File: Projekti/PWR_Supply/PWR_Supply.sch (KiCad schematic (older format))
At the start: 0 parts

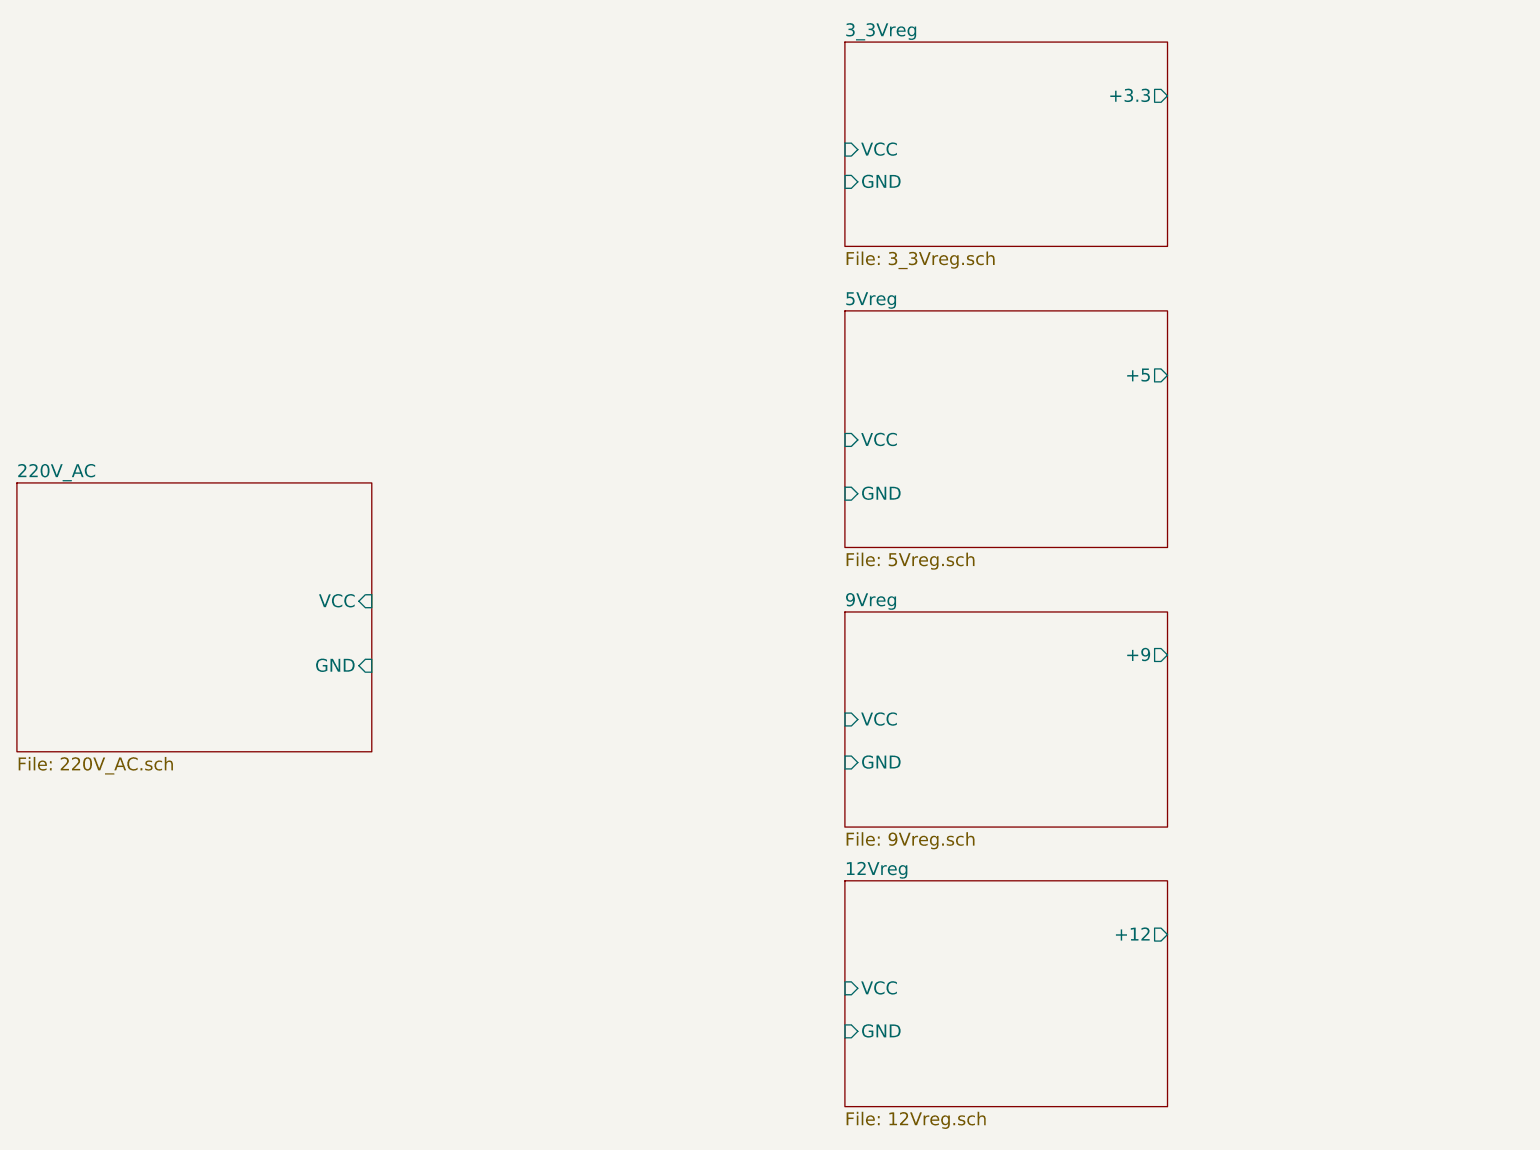
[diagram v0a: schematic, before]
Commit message: Savienojaam pin's
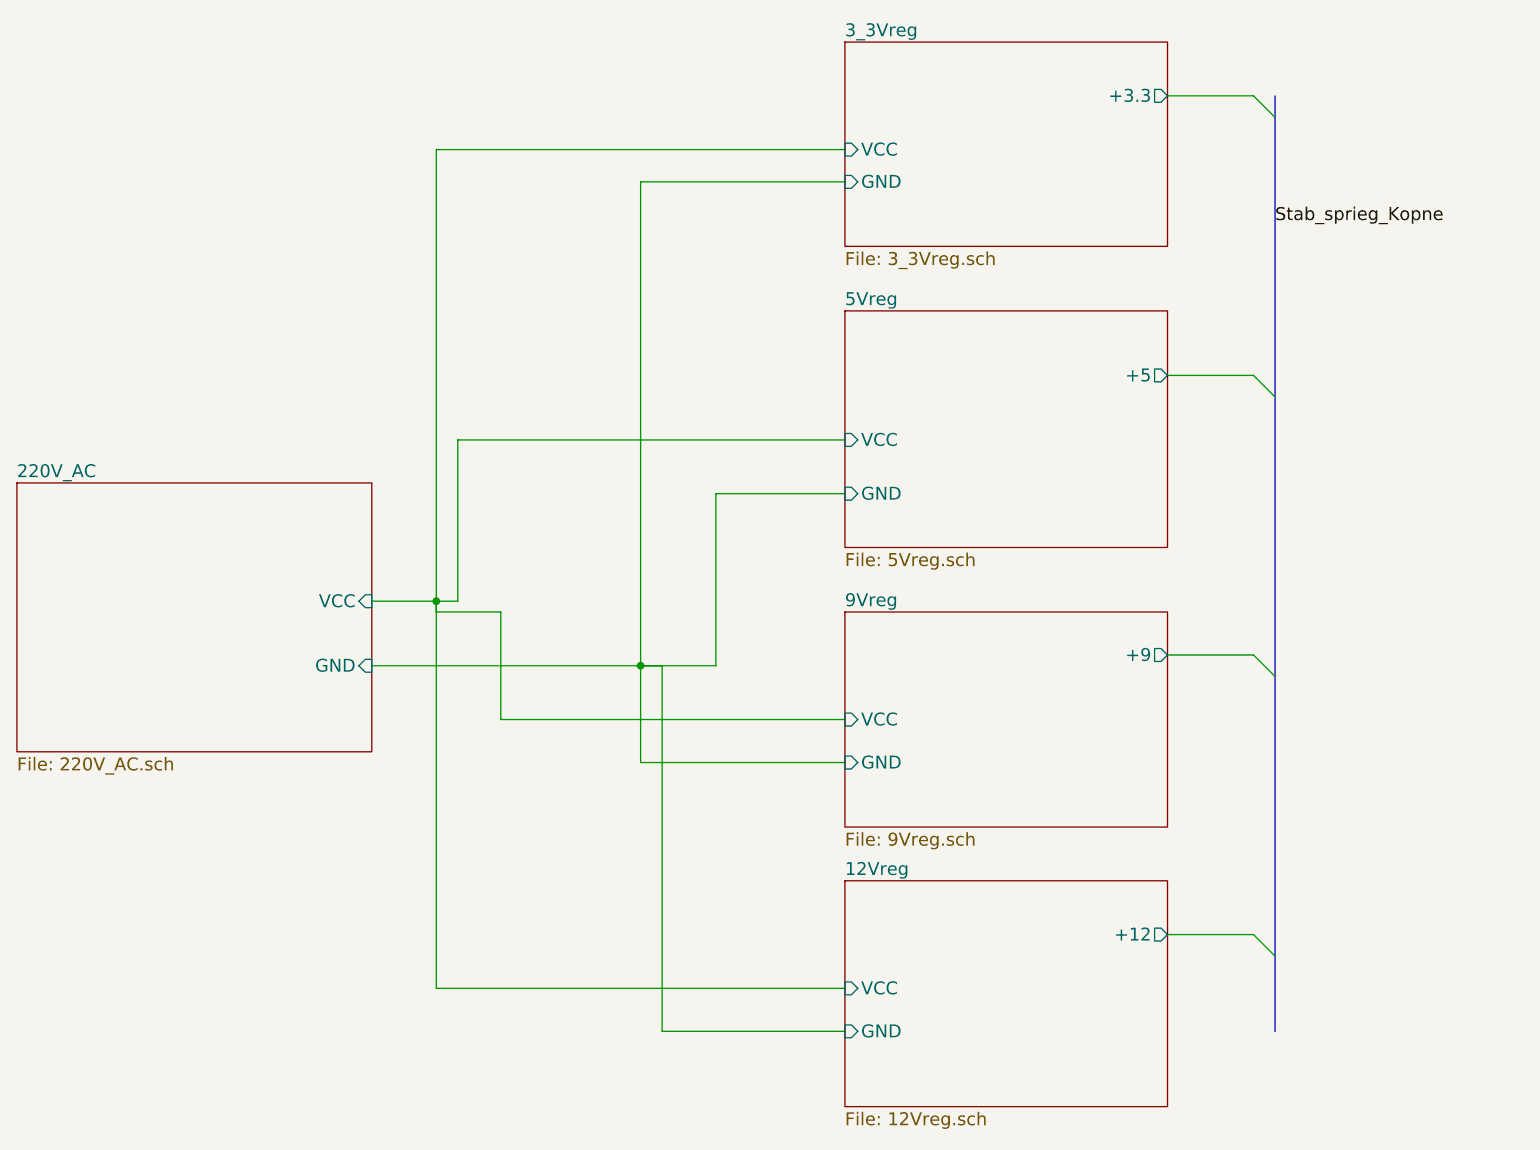
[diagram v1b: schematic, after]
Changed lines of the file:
@@
 F4 "GND" I L 7400 1950 60
 $EndSheet
+Wire Wire Line
+	7400 1800 5500 1800
+Wire Wire Line
+	5500 1800 5500 3950
+Wire Wire Line
+	5200 3900 5600 3900
+Wire Wire Line
+	7400 3150 5600 3150
+Wire Wire Line
+	5600 3150 5600 3900
+Connection ~ 5500 3900
+Wire Wire Line
+	7400 4450 5800 4450
+Wire Wire Line
+	5800 4450 5800 3950
+Wire Wire Line
+	5800 3950 5500 3950
+Wire Wire Line
+	7400 5700 5500 5700
+Wire Wire Line
+	5500 5700 5500 3900
+Wire Wire Line
+	5200 4200 6800 4200
+Wire Wire Line
+	6450 1950 6450 4650
+Wire Wire Line
+	6450 1950 7400 1950
+Wire Wire Line
+	7400 3400 6800 3400
+Wire Wire Line
+	6800 3400 6800 4200
+Connection ~ 6450 4200
+Wire Wire Line
+	6450 4650 7400 4650
+Wire Wire Line
+	7400 5900 6550 5900
+Wire Wire Line
+	6550 5900 6550 4200
+Wire Wire Line
+	6550 4200 6450 4200
+Wire Wire Line
+	8900 4150 9300 4150
+Wire Wire Line
+	8900 5450 9300 5450
+Wire Wire Line
+	8900 2850 9300 2850
+Wire Wire Line
+	8900 1550 9300 1550
+Entry Wire Line
+	9300 1550 9400 1650
+Entry Wire Line
+	9300 2850 9400 2950
+Entry Wire Line
+	9300 4150 9400 4250
+Entry Wire Line
+	9300 5450 9400 5550
+Wire Bus Line
+	9400 1550 9400 5900
+Text Label 9400 2150 0    60   ~ 0
+Stab_sprieg_Kopne
 $EndSCHEMATC

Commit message: pabeigts md ar bateriju turetajiem
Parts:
- added P2: CONN_01X04, symbol CONN_01X04
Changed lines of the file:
@@
 F0 "220V_AC" 60
 F1 "220V_AC.sch" 60
-F2 "VCC" I R 5200 3900 60
+F2 "+12V" I R 5200 3900 60
 F3 "GND" I R 5200 4200 60
 $EndSheet
@@
 F2 "+5" O R 8900 2850 60
 F3 "GND" I L 7400 3400 60
-F4 "VCC" I L 7400 3150 60
+F4 "+12V" I L 7400 3150 60
 $EndSheet
 $Sheet
@@
 F2 "+9" O R 8900 4150 60
 F3 "GND" I L 7400 4650 60
-F4 "VCC" I L 7400 4450 60
+F4 "+12V" I L 7400 4450 60
 $EndSheet
 $Sheet
@@
 F2 "+12" O R 8900 5450 60
 F3 "GND" I L 7400 5900 60
-F4 "VCC" I L 7400 5700 60
+F4 "+12V" I L 7400 5700 60
 $EndSheet
 $Sheet
@@
 F0 "3_3Vreg" 60
 F1 "3_3Vreg.sch" 60
-F2 "VCC" I L 7400 1800 60
+F2 "+12V" I L 7400 1800 60
 F3 "+3.3" O R 8900 1550 60
 F4 "GND" I L 7400 1950 60
@@
 Wire Bus Line
 	9400 1550 9400 5900
-Text Label 9400 2150 0    60   ~ 0
-Stab_sprieg_Kopne
+$Comp
+L CONN_01X04 P2
+U 1 1 58F613CD
+P 10400 2550
+F 0 "P2" H 10400 2800 50  0000 C CNN
+F 1 "CONN_01X04" V 10500 2550 50  0000 C CNN
+F 2 "" H 10400 2550 50  0000 C CNN
+F 3 "" H 10400 2550 50  0000 C CNN
+	1    10400 2550
+	1    0    0    -1
+$EndComp
+Entry Wire Line
+	9400 2300 9500 2400
+Entry Wire Line
+	9400 2400 9500 2500
+Entry Wire Line
+	9400 2500 9500 2600
+Entry Wire Line
+	9400 2600 9500 2700
+Wire Wire Line
+	9500 2400 10200 2400
+Wire Wire Line
+	9500 2500 10200 2500
+Wire Wire Line
+	9500 2600 10200 2600
+Wire Wire Line
+	9500 2700 10200 2700
 $EndSCHEMATC

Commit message: izmainas
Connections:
- net 1: now reaches P2.1 (P1)
- net 2: now reaches P2.2 (P2)
- net 3: now reaches P2.3 (P3)
- net 4: now reaches P2.4 (P4)
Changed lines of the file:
@@
 F0 "220V_AC" 60
 F1 "220V_AC.sch" 60
-F2 "+12V" I R 5200 3900 60
-F3 "GND" I R 5200 4200 60
+F2 "+12V" O R 5200 3900 60
+F3 "GND" O R 5200 4200 60
 $EndSheet
 $Sheet
@@
 F4 "GND" I L 7400 1950 60
 $EndSheet
-Wire Wire Line
-	7400 1800 5500 1800
-Wire Wire Line
-	5500 1800 5500 3950
-Wire Wire Line
-	5200 3900 5600 3900
-Wire Wire Line
-	7400 3150 5600 3150
-Wire Wire Line
-	5600 3150 5600 3900
-Connection ~ 5500 3900
-Wire Wire Line
-	7400 4450 5800 4450
-Wire Wire Line
-	5800 4450 5800 3950
-Wire Wire Line
-	5800 3950 5500 3950
-Wire Wire Line
-	7400 5700 5500 5700
-Wire Wire Line
-	5500 5700 5500 3900
-Wire Wire Line
-	5200 4200 6800 4200
-Wire Wire Line
-	6450 1950 6450 4650
-Wire Wire Line
-	6450 1950 7400 1950
-Wire Wire Line
-	7400 3400 6800 3400
-Wire Wire Line
-	6800 3400 6800 4200
-Connection ~ 6450 4200
-Wire Wire Line
-	6450 4650 7400 4650
-Wire Wire Line
-	7400 5900 6550 5900
-Wire Wire Line
-	6550 5900 6550 4200
-Wire Wire Line
-	6550 4200 6450 4200
-Wire Wire Line
-	8900 4150 9300 4150
-Wire Wire Line
-	8900 5450 9300 5450
-Wire Wire Line
-	8900 2850 9300 2850
-Wire Wire Line
-	8900 1550 9300 1550
 Entry Wire Line
 	9300 1550 9400 1650
@@
 Entry Wire Line
 	9300 5450 9400 5550
-Wire Bus Line
-	9400 1550 9400 5900
 $Comp
 L CONN_01X04 P2
@@
 Entry Wire Line
 	9400 2600 9500 2700
+Text Label 10100 2400 0    60   ~ 0
+1
+Text Label 9200 1550 0    60   ~ 0
+1
+Text Label 10100 2500 0    60   ~ 0
+2
+Text Label 9200 2850 0    60   ~ 0
+2
+Text Label 10100 2600 0    60   ~ 0
+3
+Text Label 9200 4150 0    60   ~ 0
+3
+Text Label 10100 2700 0    60   ~ 0
+4
+Text Label 9250 5450 0    60   ~ 0
+4
+$Comp
+L PWR_FLAG #FLG01
+U 1 1 5943FB49
+P 5350 3800
+F 0 "#FLG01" H 5350 3895 50  0001 C CNN
+F 1 "PWR_FLAG" H 5350 3980 50  0000 C CNN
+F 2 "" H 5350 3800 50  0000 C CNN
+F 3 "" H 5350 3800 50  0000 C CNN
+	1    5350 3800
+	1    0    0    -1
+$EndComp
+$Comp
+L PWR_FLAG #FLG02
+U 1 1 59443C0E
+P 5350 4400
+F 0 "#FLG02" H 5350 4495 50  0001 C CNN
+F 1 "PWR_FLAG" H 5350 4580 50  0000 C CNN
+F 2 "" H 5350 4400 50  0000 C CNN
+F 3 "" H 5350 4400 50  0000 C CNN
+	1    5350 4400
+	-1   0    0    1
+$EndComp
+Entry Wire Line
+	6050 3900 6150 4000
+Entry Wire Line
+	6150 3700 6250 3800
+Entry Wire Line
+	6150 3800 6250 3900
+Entry Wire Line
+	6150 3950 6250 4050
+Entry Wire Line
+	6150 4050 6250 4150
+Entry Wire Line
+	5550 4200 5650 4300
+Entry Wire Line
+	5650 4200 5750 4300
+Entry Wire Line
+	5650 4400 5750 4500
+Entry Wire Line
+	5650 4500 5750 4600
+Entry Wire Line
+	5650 4650 5750 4750
+Wire Wire Line
+	8900 4150 9300 4150
+Wire Wire Line
+	8900 5450 9300 5450
+Wire Wire Line
+	8900 2850 9300 2850
+Wire Wire Line
+	8900 1550 9300 1550
+Wire Bus Line
+	9400 1550 9400 5900
 Wire Wire Line
 	9500 2400 10200 2400
@@
 Wire Wire Line
 	9500 2700 10200 2700
+Wire Wire Line
+	5350 3800 5350 3900
+Connection ~ 5350 3900
+Wire Wire Line
+	5350 4400 5350 4200
+Connection ~ 5350 4200
+Wire Wire Line
+	5200 3900 6050 3900
+Wire Bus Line
+	6150 4100 6150 3650
+Wire Wire Line
+	7400 1800 6250 1800
+Wire Wire Line
+	6250 1800 6250 3800
+Wire Wire Line
+	7400 3150 6400 3150
+Wire Wire Line
+	6400 3150 6400 3900
+Wire Wire Line
+	6400 3900 6250 3900
+Wire Wire Line
+	7400 4450 6400 4450
+Wire Wire Line
+	6400 4450 6400 4050
+Wire Wire Line
+	6400 4050 6250 4050
+Wire Wire Line
+	7400 5700 6250 5700
+Wire Wire Line
+	6250 5700 6250 4150
+Wire Wire Line
+	5200 4200 5550 4200
+Wire Bus Line
+	5650 4100 5650 4650
+Wire Wire Line
+	7400 1950 6500 1950
+Wire Wire Line
+	6500 1950 6500 4300
+Wire Wire Line
+	6500 4300 5750 4300
+Wire Wire Line
+	5750 4500 7200 4500
+Wire Wire Line
+	7200 4500 7200 3400
+Wire Wire Line
+	7200 3400 7400 3400
+Wire Wire Line
+	5750 4750 6100 4750
+Wire Wire Line
+	6100 4750 6100 5900
+Wire Wire Line
+	6100 5900 7400 5900
+Wire Wire Line
+	5750 4600 7300 4600
+Wire Wire Line
+	7300 4600 7300 4650
+Wire Wire Line
+	7300 4650 7400 4650
 $EndSCHEMATC
